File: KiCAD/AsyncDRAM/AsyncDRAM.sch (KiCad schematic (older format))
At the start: 14 parts, among them J1 UART, J2 SPI, J3 UPDI, J4 POWER

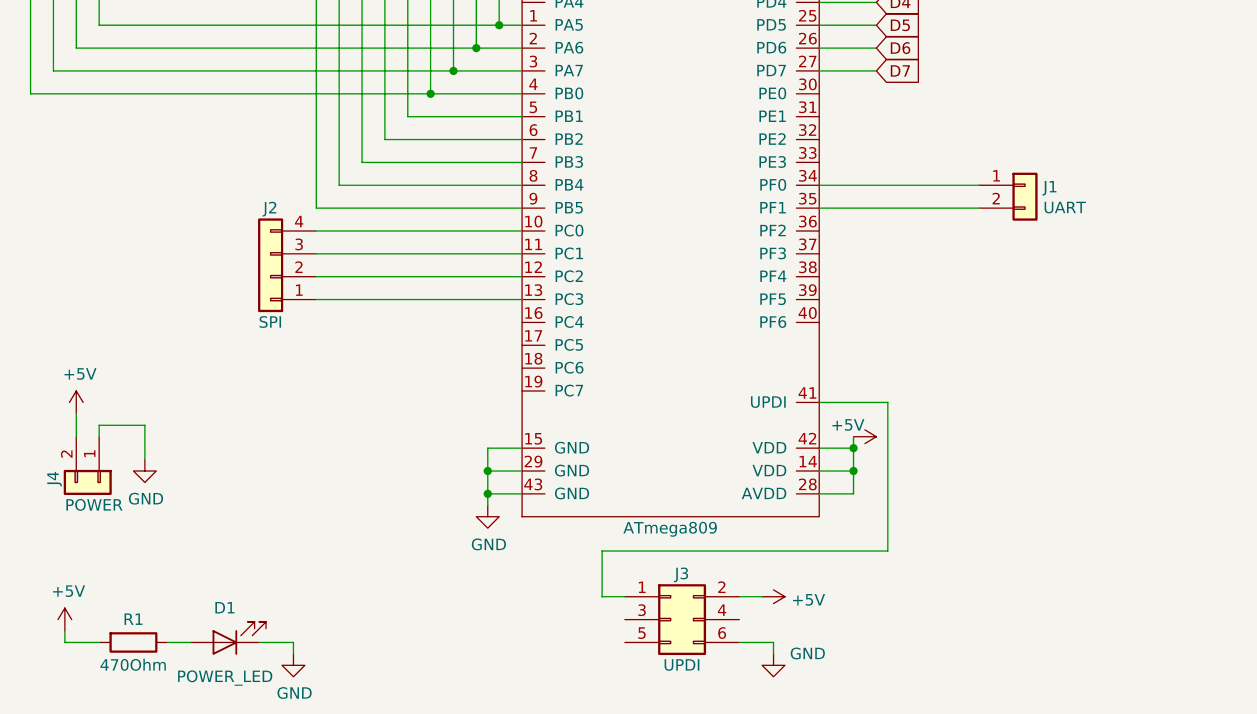
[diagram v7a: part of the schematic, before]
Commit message: Added Library for SMD LEDs, updated PCB
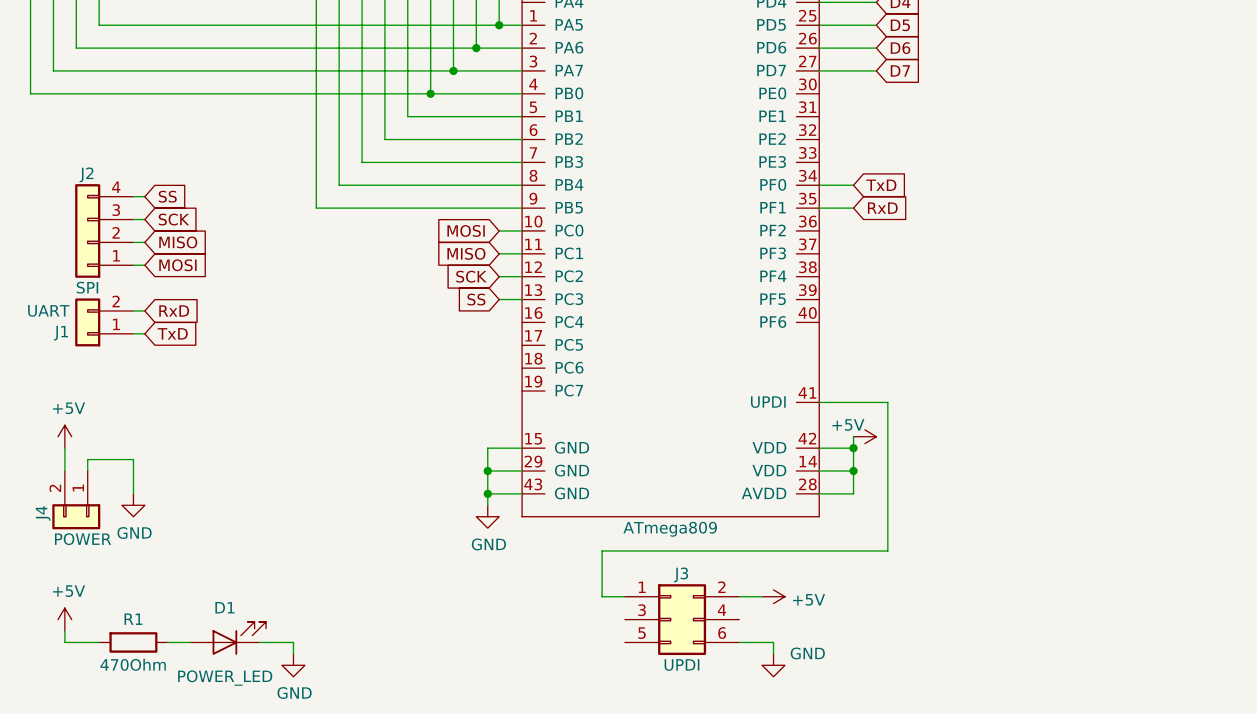
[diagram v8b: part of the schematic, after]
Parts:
- C1, C2, C3, C4, C5: footprint (none) -> CapacitorSMD:C_0805_2012Metric
- D1: footprint (none) -> LEDSMD:LED_1206_3216Metric
- J1, J4: footprint (none) -> ConnectorPinHeader:PinHeader_1x02_P2.54mm_Vertical
- J2: footprint (none) -> ConnectorPinHeader:PinHeader_1x04_P2.54mm_Vertical
- J3: footprint (none) -> ConnectorPinHeader:PinHeader_2x03_P2.54mm_Vertical
- KM44256_1, KM44256_2: footprint (none) -> DIP:DIP-20_W7.62mm
- R1: footprint (none) -> ResistorSMD:R_0805_2012Metric
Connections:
- net MOSI: now reaches ATM809_1.10 (PC0)
- net MOSI: now also J2.1 (Pin_1); no longer J2.4 (Pin_4)
- net MISO: now reaches ATM809_1.11 (PC1)
- net MISO: now also J2.2 (Pin_2); no longer J2.3 (Pin_3)
- net SCK: now reaches ATM809_1.12 (PC2)
- net SCK: now also J2.3 (Pin_3); no longer J2.2 (Pin_2)
- net SS: now reaches ATM809_1.13 (PC3)
- net SS: now also J2.4 (Pin_4); no longer J2.1 (Pin_1)
- net TxD: now reaches ATM809_1.34 (PF0), J1.1 (Pin_1)
- net RxD: now reaches ATM809_1.35 (PF1), J1.2 (Pin_2)
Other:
- moved on the sheet: J1, J2, J4
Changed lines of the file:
@@
 F 0 "KM44256_2" H 1250 1950 50  0000 C CNN
 F 1 "KM44C256BP-8" H 1250 750 50  0000 C CNN
-F 2 "" H 1200 1450 50  0001 C CNN
+F 2 "DIP:DIP-20_W7.62mm" H 1200 1450 50  0001 C CNN
 F 3 "" H 1200 1450 50  0001 C CNN
 	1    1250 1350
@@
 F 0 "C1" H 1025 6800 50  0000 L CNN
 F 1 "100nF" H 1025 6600 50  0000 L CNN
-F 2 "" H 1038 6550 50  0001 C CNN
+F 2 "CapacitorSMD:C_0805_2012Metric" H 1038 6550 50  0001 C CNN
 F 3 "~" H 1000 6700 50  0001 C CNN
 	1    1000 6700
@@
 F 0 "C2" H 1025 7050 50  0000 L CNN
 F 1 "100nF" H 1025 6850 50  0000 L CNN
-F 2 "" H 1038 6800 50  0001 C CNN
+F 2 "CapacitorSMD:C_0805_2012Metric" H 1038 6800 50  0001 C CNN
 F 3 "~" H 1000 6950 50  0001 C CNN
 	1    1000 6950
@@
 F 0 "C4" H 1925 6800 50  0000 L CNN
 F 1 "47µF" H 1925 6600 50  0000 L CNN
-F 2 "" H 1938 6550 50  0001 C CNN
+F 2 "CapacitorSMD:C_0805_2012Metric" H 1938 6550 50  0001 C CNN
 F 3 "~" H 1900 6700 50  0001 C CNN
 	1    1900 6700
@@
 F 0 "C5" H 1925 7050 50  0000 L CNN
 F 1 "47µF" H 1925 6850 50  0000 L CNN
-F 2 "" H 1938 6800 50  0001 C CNN
+F 2 "CapacitorSMD:C_0805_2012Metric" H 1938 6800 50  0001 C CNN
 F 3 "~" H 1900 6950 50  0001 C CNN
 	1    1900 6950
@@
 F 0 "KM44256_1" H 5250 2200 50  0000 C CNN
 F 1 "KM44C256BP-8" H 5250 1000 50  0000 C CNN
-F 2 "" H 5200 1700 50  0001 C CNN
+F 2 "DIP:DIP-20_W7.62mm" H 5200 1700 50  0001 C CNN
 F 3 "" H 5200 1700 50  0001 C CNN
 	1    5250 1600
@@
 F 0 "C3" H 1025 7300 50  0000 L CNN
 F 1 "100nF" H 1025 7100 50  0000 L CNN
-F 2 "" H 1038 7050 50  0001 C CNN
+F 2 "CapacitorSMD:C_0805_2012Metric" H 1038 7050 50  0001 C CNN
 F 3 "~" H 1000 7200 50  0001 C CNN
 	1    1000 7200
@@
 F 0 "D1" H 1350 5600 50  0000 C CNN
 F 1 "POWER_LED" H 1350 5900 50  0000 C CNN
-F 2 "" H 1350 5750 50  0001 C CNN
+F 2 "LEDSMD:LED_1206_3216Metric" H 1350 5750 50  0001 C CNN
 F 3 "~" H 1350 5750 50  0001 C CNN
 	1    1350 5750
@@
 $EndComp
 $Comp
-L Power:+5V #PWR?
+L Power:+5V #PWR0111
 U 1 1 5DAE0A34
 P 650 5700
-F 0 "#PWR?" H 650 5550 50  0001 C CNN
+F 0 "#PWR0111" H 650 5550 50  0001 C CNN
 F 1 "+5V" H 665 5873 50  0000 C CNN
 F 2 "" H 650 5700 50  0001 C CNN
@@
 $EndComp
 $Comp
-L Power:GND #PWR?
+L Power:GND #PWR0112
 U 1 1 5DAE0D3A
 P 1650 5800
-F 0 "#PWR?" H 1650 5550 50  0001 C CNN
+F 0 "#PWR0112" H 1650 5550 50  0001 C CNN
 F 1 "GND" H 1655 5627 50  0000 C CNN
 F 2 "" H 1650 5800 50  0001 C CNN
@@
 L Connectors_Generic:Conn_01x02 J1
 U 1 1 5DC15064
-P 4850 3750
-F 0 "J1" H 4930 3742 50  0000 L CNN
-F 1 "UART" H 4930 3651 50  0000 L CNN
-F 2 "" H 4850 3750 50  0001 C CNN
-F 3 "~" H 4850 3750 50  0001 C CNN
-	1    4850 3750
-	1    0    0    -1
+P 750 4400
+F 0 "J1" H 830 4392 50  0000 L CNN
+F 1 "UART" H 830 4301 50  0000 L CNN
+F 2 "ConnectorPinHeader:PinHeader_1x02_P2.54mm_Vertical" H 750 4400 50  0001 C CNN
+F 3 "~" H 750 4400 50  0001 C CNN
+	1    750  4400
+	-1   0    0    1
 $EndComp
 $Comp
 L Connectors_Generic:Conn_01x04 J2
 U 1 1 5DC178D1
-P 1550 4150
-F 0 "J2" H 1550 3850 50  0000 C CNN
-F 1 "SPI" H 1550 4350 50  0000 C CNN
-F 2 "" H 1550 4150 50  0001 C CNN
-F 3 "~" H 1550 4150 50  0001 C CNN
-	1    1550 4150
+P 750 4000
+F 0 "J2" H 750 3700 50  0000 C CNN
+F 1 "SPI" H 750 4200 50  0000 C CNN
+F 2 "ConnectorPinHeader:PinHeader_1x04_P2.54mm_Vertical" H 750 4000 50  0001 C CNN
+F 3 "~" H 750 4000 50  0001 C CNN
+	1    750  4000
 	-1   0    0    1
 $EndComp
 Wire Wire Line
 	1500 5750 1650 5750
-Wire Wire Line
-	1750 3950 2650 3950
-Wire Wire Line
-	1750 4050 2650 4050
-Wire Wire Line
-	1750 4150 2650 4150
-Wire Wire Line
-	1750 4250 2650 4250
-Wire Wire Line
-	3950 3750 4650 3750
-Wire Wire Line
-	4650 3850 3950 3850
 $Comp
 L Connectors_Generic:Conn_02x03_Odd_Even J3
@@
 F 0 "J3" H 3350 5850 50  0000 C CNN
 F 1 "UPDI" H 3350 5450 50  0000 C CNN
-F 2 "" H 3300 5650 50  0001 C CNN
+F 2 "ConnectorPinHeader:PinHeader_2x03_P2.54mm_Vertical" H 3300 5650 50  0001 C CNN
 F 3 "~" H 3300 5650 50  0001 C CNN
 	1    3300 5650
@@
 	3000 5550 3100 5550
 $Comp
-L Power:+5V #PWR?
+L Power:+5V #PWR0113
 U 1 1 5DC495AA
 P 3700 5550
-F 0 "#PWR?" H 3700 5400 50  0001 C CNN
+F 0 "#PWR0113" H 3700 5400 50  0001 C CNN
 F 1 "+5V" V 3715 5678 50  0000 L CNN
 F 2 "" H 3700 5550 50  0001 C CNN
@@
 	3600 5550 3700 5550
 $Comp
-L Power:GND #PWR?
+L Power:GND #PWR0114
 U 1 1 5DC4DA60
 P 3750 5800
-F 0 "#PWR?" H 3750 5550 50  0001 C CNN
+F 0 "#PWR0114" H 3750 5550 50  0001 C CNN
 F 1 "GND" H 3900 5800 50  0000 C CNN
 F 2 "" H 3750 5800 50  0001 C CNN
@@
 L Connectors_Generic:Conn_01x02 J4
 U 1 1 5DD828A4
-P 800 5050
-F 0 "J4" H 750 4850 50  0000 L CNN
-F 1 "POWER" V 900 4900 50  0000 L CNN
-F 2 "" H 800 5050 50  0001 C CNN
-F 3 "~" H 800 5050 50  0001 C CNN
-	1    800  5050
-	0    1    1    0
-$EndComp
-$Comp
-L Power:+5V #PWR?
+P 750 5200
+F 0 "J4" H 700 5000 50  0000 L CNN
+F 1 "POWER" V 850 5050 50  0000 L CNN
+F 2 "ConnectorPinHeader:PinHeader_1x02_P2.54mm_Vertical" H 750 5200 50  0001 C CNN
+F 3 "~" H 750 5200 50  0001 C CNN
+	1    750  5200
+	0    1    1    0
+$EndComp
+$Comp
+L Power:+5V #PWR0115
 U 1 1 5DD836CE
-P 700 4750
-F 0 "#PWR?" H 700 4600 50  0001 C CNN
-F 1 "+5V" H 715 4923 50  0000 C CNN
-F 2 "" H 700 4750 50  0001 C CNN
-F 3 "" H 700 4750 50  0001 C CNN
-	1    700  4750
-	1    0    0    -1
-$EndComp
-$Comp
-L Power:GND #PWR?
+P 650 4900
+F 0 "#PWR0115" H 650 4750 50  0001 C CNN
+F 1 "+5V" H 665 5073 50  0000 C CNN
+F 2 "" H 650 4900 50  0001 C CNN
+F 3 "" H 650 4900 50  0001 C CNN
+	1    650  4900
+	1    0    0    -1
+$EndComp
+$Comp
+L Power:GND #PWR0116
 U 1 1 5DD83A8E
-P 1000 4950
-F 0 "#PWR?" H 1000 4700 50  0001 C CNN
-F 1 "GND" H 1005 4777 50  0000 C CNN
-F 2 "" H 1000 4950 50  0001 C CNN
-F 3 "" H 1000 4950 50  0001 C CNN
-	1    1000 4950
-	1    0    0    -1
-$EndComp
-Wire Wire Line
-	800  4850 800  4800
-Wire Wire Line
-	800  4800 1000 4800
-Wire Wire Line
-	1000 4800 1000 4950
-Wire Wire Line
-	700  4850 700  4750
+P 950 5100
+F 0 "#PWR0116" H 950 4850 50  0001 C CNN
+F 1 "GND" H 955 4927 50  0000 C CNN
+F 2 "" H 950 5100 50  0001 C CNN
+F 3 "" H 950 5100 50  0001 C CNN
+	1    950  5100
+	1    0    0    -1
+$EndComp
+Wire Wire Line
+	750  5000 750  4950
+Wire Wire Line
+	750  4950 950  4950
+Wire Wire Line
+	950  4950 950  5100
+Wire Wire Line
+	650  5000 650  4900
 $Comp
 L Device:R R1
@@
 F 0 "R1" V 850 5750 50  0000 C CNN
 F 1 "470Ohm" V 1050 5750 50  0000 C CNN
-F 2 "" V 880 5750 50  0001 C CNN
+F 2 "ResistorSMD:R_0805_2012Metric" V 880 5750 50  0001 C CNN
 F 3 "~" H 950 5750 50  0001 C CNN
 	1    950  5750
@@
 Text Notes 3000 7250 0    50   ~ 0
 (PA5, PA6, PA7, PB0, PB1, PB2, PB3, PB4, PB5)
+Text GLabel 2550 3950 0    50   Input ~ 0
+MOSI
+Text GLabel 2550 4050 0    50   Input ~ 0
+MISO
+Text GLabel 2550 4150 0    50   Input ~ 0
+SCK
+Text GLabel 2550 4250 0    50   Input ~ 0
+SS
+Wire Wire Line
+	2550 3950 2650 3950
+Wire Wire Line
+	2550 4050 2650 4050
+Wire Wire Line
+	2550 4150 2650 4150
+Wire Wire Line
+	2550 4250 2650 4250
+Text GLabel 1000 4100 2    50   Input ~ 0
+MOSI
+Text GLabel 1000 4000 2    50   Input ~ 0
+MISO
+Text GLabel 1000 3900 2    50   Input ~ 0
+SCK
+Text GLabel 1000 3800 2    50   Input ~ 0
+SS
+Wire Wire Line
+	950  3800 1000 3800
+Wire Wire Line
+	950  3900 1000 3900
+Wire Wire Line
+	950  4000 1000 4000
+Wire Wire Line
+	950  4100 1000 4100
+Text GLabel 4100 3750 2    50   Input ~ 0
+TxD
+Text GLabel 4100 3850 2    50   Input ~ 0
+RxD
+Wire Wire Line
+	4100 3750 3950 3750
+Wire Wire Line
+	4100 3850 3950 3850
+Text GLabel 1000 4400 2    50   Input ~ 0
+TxD
+Text GLabel 1000 4300 2    50   Input ~ 0
+RxD
+Wire Wire Line
+	1000 4400 950  4400
+Wire Wire Line
+	1000 4300 950  4300
 $EndSCHEMATC
